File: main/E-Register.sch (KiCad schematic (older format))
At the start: 19 parts, among them U71 74LS245, U72 74LS173, U73 74LS173

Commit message: Replot main with symbols
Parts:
- renumbered D46 to D38, D47 to D39, D48 to D40, D49 to D41, D50 to D42, D51 to D43, D52 to D44, D53 to D45, R52 to R44, R53 to R45, R54 to R46, R55 to R47, R56 to R48, R57 to R49, R58 to R50, R59 to R51, U71 to U56, U72 to U57, U73 to U58
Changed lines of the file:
@@
 Sheet 15 26
 Title "E Register"
-Date "2019-11-13"
+Date "2019-11-17"
 Rev "v1.0"
 Comp "Christopher Milan"
@@
 AR Path="/5D9C73BD/5DA2C3AD" Ref="U?"  Part="1"
 AR Path="/5D9E8388/5DA2C3AD" Ref="U?"  Part="1"
-AR Path="/5DA98D6D/5DA9A55B/5DA2C3AD" Ref="U71"  Part="1"
-F 0 "U71" V 2946 2156 50  0000 R CNN
+AR Path="/5DA98D6D/5DA9A55B/5DA2C3AD" Ref="U56"  Part="1"
+F 0 "U56" V 2946 2156 50  0000 R CNN
 F 1 "74LS245" V 2855 2156 50  0000 R CNN
 F 2 "" H 2900 3000 50  0001 C CNN
@@
 AR Path="/5D9C73BD/5DA2C3DA" Ref="U?"  Part="1"
 AR Path="/5D9E8388/5DA2C3DA" Ref="U?"  Part="1"
-AR Path="/5DA98D6D/5DA9A55B/5DA2C3DA" Ref="U73"  Part="1"
-F 0 "U73" V 7454 3944 50  0000 L CNN
+AR Path="/5DA98D6D/5DA9A55B/5DA2C3DA" Ref="U58"  Part="1"
+F 0 "U58" V 7454 3944 50  0000 L CNN
 F 1 "74LS173" V 7545 3944 50  0000 L CNN
 F 2 "" H 7500 3000 50  0001 C CNN
@@
 AR Path="/5D9C73BD/5DA2C404" Ref="D?"  Part="1"
 AR Path="/5D9E8388/5DA2C404" Ref="D?"  Part="1"
-AR Path="/5DA98D6D/5DA9A55B/5DA2C404" Ref="D46"  Part="1"
-F 0 "D46" V 3489 5383 50  0000 R CNN
+AR Path="/5DA98D6D/5DA9A55B/5DA2C404" Ref="D38"  Part="1"
+F 0 "D38" V 3489 5383 50  0000 R CNN
 F 1 "LED" V 3398 5383 50  0000 R CNN
 F 2 "" H 3450 5500 50  0001 C CNN
@@
 AR Path="/5D9C73BD/5DA2C40A" Ref="D?"  Part="1"
 AR Path="/5D9E8388/5DA2C40A" Ref="D?"  Part="1"
-AR Path="/5DA98D6D/5DA9A55B/5DA2C40A" Ref="D47"  Part="1"
-F 0 "D47" V 3839 5383 50  0000 R CNN
+AR Path="/5DA98D6D/5DA9A55B/5DA2C40A" Ref="D39"  Part="1"
+F 0 "D39" V 3839 5383 50  0000 R CNN
 F 1 "LED" V 3748 5383 50  0000 R CNN
 F 2 "" H 3800 5500 50  0001 C CNN
@@
 AR Path="/5D9C73BD/5DA2C410" Ref="D?"  Part="1"
 AR Path="/5D9E8388/5DA2C410" Ref="D?"  Part="1"
-AR Path="/5DA98D6D/5DA9A55B/5DA2C410" Ref="D48"  Part="1"
-F 0 "D48" V 4189 5383 50  0000 R CNN
+AR Path="/5DA98D6D/5DA9A55B/5DA2C410" Ref="D40"  Part="1"
+F 0 "D40" V 4189 5383 50  0000 R CNN
 F 1 "LED" V 4098 5383 50  0000 R CNN
 F 2 "" H 4150 5500 50  0001 C CNN
@@
 AR Path="/5D9C73BD/5DA2C416" Ref="D?"  Part="1"
 AR Path="/5D9E8388/5DA2C416" Ref="D?"  Part="1"
-AR Path="/5DA98D6D/5DA9A55B/5DA2C416" Ref="D49"  Part="1"
-F 0 "D49" V 4539 5383 50  0000 R CNN
+AR Path="/5DA98D6D/5DA9A55B/5DA2C416" Ref="D41"  Part="1"
+F 0 "D41" V 4539 5383 50  0000 R CNN
 F 1 "LED" V 4448 5383 50  0000 R CNN
 F 2 "" H 4500 5500 50  0001 C CNN
@@
 AR Path="/5D9C73BD/5DA2C41C" Ref="D?"  Part="1"
 AR Path="/5D9E8388/5DA2C41C" Ref="D?"  Part="1"
-AR Path="/5DA98D6D/5DA9A55B/5DA2C41C" Ref="D50"  Part="1"
-F 0 "D50" V 4889 5383 50  0000 R CNN
+AR Path="/5DA98D6D/5DA9A55B/5DA2C41C" Ref="D42"  Part="1"
+F 0 "D42" V 4889 5383 50  0000 R CNN
 F 1 "LED" V 4798 5383 50  0000 R CNN
 F 2 "" H 4850 5500 50  0001 C CNN
@@
 AR Path="/5D9C73BD/5DA2C422" Ref="D?"  Part="1"
 AR Path="/5D9E8388/5DA2C422" Ref="D?"  Part="1"
-AR Path="/5DA98D6D/5DA9A55B/5DA2C422" Ref="D51"  Part="1"
-F 0 "D51" V 5239 5383 50  0000 R CNN
+AR Path="/5DA98D6D/5DA9A55B/5DA2C422" Ref="D43"  Part="1"
+F 0 "D43" V 5239 5383 50  0000 R CNN
 F 1 "LED" V 5148 5383 50  0000 R CNN
 F 2 "" H 5200 5500 50  0001 C CNN
@@
 AR Path="/5D9C73BD/5DA2C428" Ref="D?"  Part="1"
 AR Path="/5D9E8388/5DA2C428" Ref="D?"  Part="1"
-AR Path="/5DA98D6D/5DA9A55B/5DA2C428" Ref="D52"  Part="1"
-F 0 "D52" V 5589 5383 50  0000 R CNN
+AR Path="/5DA98D6D/5DA9A55B/5DA2C428" Ref="D44"  Part="1"
+F 0 "D44" V 5589 5383 50  0000 R CNN
 F 1 "LED" V 5498 5383 50  0000 R CNN
 F 2 "" H 5550 5500 50  0001 C CNN
@@
 AR Path="/5D9C73BD/5DA2C42E" Ref="D?"  Part="1"
 AR Path="/5D9E8388/5DA2C42E" Ref="D?"  Part="1"
-AR Path="/5DA98D6D/5DA9A55B/5DA2C42E" Ref="D53"  Part="1"
-F 0 "D53" V 5939 5383 50  0000 R CNN
+AR Path="/5DA98D6D/5DA9A55B/5DA2C42E" Ref="D45"  Part="1"
+F 0 "D45" V 5939 5383 50  0000 R CNN
 F 1 "LED" V 5848 5383 50  0000 R CNN
 F 2 "" H 5900 5500 50  0001 C CNN
@@
 AR Path="/5D9C73BD/5DA2C44A" Ref="R?"  Part="1"
 AR Path="/5D9E8388/5DA2C44A" Ref="R?"  Part="1"
-AR Path="/5DA98D6D/5DA9A55B/5DA2C44A" Ref="R52"  Part="1"
-F 0 "R52" H 3520 6096 50  0000 L CNN
+AR Path="/5DA98D6D/5DA9A55B/5DA2C44A" Ref="R44"  Part="1"
+F 0 "R44" H 3520 6096 50  0000 L CNN
 F 1 "220" H 3520 6005 50  0000 L CNN
 F 2 "" V 3380 6050 50  0001 C CNN
@@
 AR Path="/5D9C73BD/5DA2C450" Ref="R?"  Part="1"
 AR Path="/5D9E8388/5DA2C450" Ref="R?"  Part="1"
-AR Path="/5DA98D6D/5DA9A55B/5DA2C450" Ref="R53"  Part="1"
-F 0 "R53" H 3870 6096 50  0000 L CNN
+AR Path="/5DA98D6D/5DA9A55B/5DA2C450" Ref="R45"  Part="1"
+F 0 "R45" H 3870 6096 50  0000 L CNN
 F 1 "220" H 3870 6005 50  0000 L CNN
 F 2 "" V 3730 6050 50  0001 C CNN
@@
 AR Path="/5D9C73BD/5DA2C456" Ref="R?"  Part="1"
 AR Path="/5D9E8388/5DA2C456" Ref="R?"  Part="1"
-AR Path="/5DA98D6D/5DA9A55B/5DA2C456" Ref="R54"  Part="1"
-F 0 "R54" H 4220 6096 50  0000 L CNN
+AR Path="/5DA98D6D/5DA9A55B/5DA2C456" Ref="R46"  Part="1"
+F 0 "R46" H 4220 6096 50  0000 L CNN
 F 1 "220" H 4220 6005 50  0000 L CNN
 F 2 "" V 4080 6050 50  0001 C CNN
@@
 AR Path="/5D9C73BD/5DA2C45C" Ref="R?"  Part="1"
 AR Path="/5D9E8388/5DA2C45C" Ref="R?"  Part="1"
-AR Path="/5DA98D6D/5DA9A55B/5DA2C45C" Ref="R55"  Part="1"
-F 0 "R55" H 4570 6096 50  0000 L CNN
+AR Path="/5DA98D6D/5DA9A55B/5DA2C45C" Ref="R47"  Part="1"
+F 0 "R47" H 4570 6096 50  0000 L CNN
 F 1 "220" H 4570 6005 50  0000 L CNN
 F 2 "" V 4430 6050 50  0001 C CNN
@@
 AR Path="/5D9C73BD/5DA2C462" Ref="R?"  Part="1"
 AR Path="/5D9E8388/5DA2C462" Ref="R?"  Part="1"
-AR Path="/5DA98D6D/5DA9A55B/5DA2C462" Ref="R56"  Part="1"
-F 0 "R56" H 4920 6096 50  0000 L CNN
+AR Path="/5DA98D6D/5DA9A55B/5DA2C462" Ref="R48"  Part="1"
+F 0 "R48" H 4920 6096 50  0000 L CNN
 F 1 "220" H 4920 6005 50  0000 L CNN
 F 2 "" V 4780 6050 50  0001 C CNN
@@
 AR Path="/5D9C73BD/5DA2C468" Ref="R?"  Part="1"
 AR Path="/5D9E8388/5DA2C468" Ref="R?"  Part="1"
-AR Path="/5DA98D6D/5DA9A55B/5DA2C468" Ref="R57"  Part="1"
-F 0 "R57" H 5270 6096 50  0000 L CNN
+AR Path="/5DA98D6D/5DA9A55B/5DA2C468" Ref="R49"  Part="1"
+F 0 "R49" H 5270 6096 50  0000 L CNN
 F 1 "220" H 5270 6005 50  0000 L CNN
 F 2 "" V 5130 6050 50  0001 C CNN
@@
 AR Path="/5D9C73BD/5DA2C46E" Ref="R?"  Part="1"
 AR Path="/5D9E8388/5DA2C46E" Ref="R?"  Part="1"
-AR Path="/5DA98D6D/5DA9A55B/5DA2C46E" Ref="R58"  Part="1"
-F 0 "R58" H 5620 6096 50  0000 L CNN
+AR Path="/5DA98D6D/5DA9A55B/5DA2C46E" Ref="R50"  Part="1"
+F 0 "R50" H 5620 6096 50  0000 L CNN
 F 1 "220" H 5620 6005 50  0000 L CNN
 F 2 "" V 5480 6050 50  0001 C CNN
@@
 AR Path="/5D9C73BD/5DA2C474" Ref="R?"  Part="1"
 AR Path="/5D9E8388/5DA2C474" Ref="R?"  Part="1"
-AR Path="/5DA98D6D/5DA9A55B/5DA2C474" Ref="R59"  Part="1"
-F 0 "R59" H 5970 6096 50  0000 L CNN
+AR Path="/5DA98D6D/5DA9A55B/5DA2C474" Ref="R51"  Part="1"
+F 0 "R51" H 5970 6096 50  0000 L CNN
 F 1 "220" H 5970 6005 50  0000 L CNN
 F 2 "" V 5830 6050 50  0001 C CNN
@@
 AR Path="/5D9C73BD/5DA2C4C5" Ref="U?"  Part="1"
 AR Path="/5D9E8388/5DA2C4C5" Ref="U?"  Part="1"
-AR Path="/5DA98D6D/5DA9A55B/5DA2C4C5" Ref="U72"  Part="1"
-F 0 "U72" V 5204 3944 50  0000 L CNN
+AR Path="/5DA98D6D/5DA9A55B/5DA2C4C5" Ref="U57"  Part="1"
+F 0 "U57" V 5204 3944 50  0000 L CNN
 F 1 "74LS173" V 5295 3944 50  0000 L CNN
 F 2 "" H 5250 3000 50  0001 C CNN

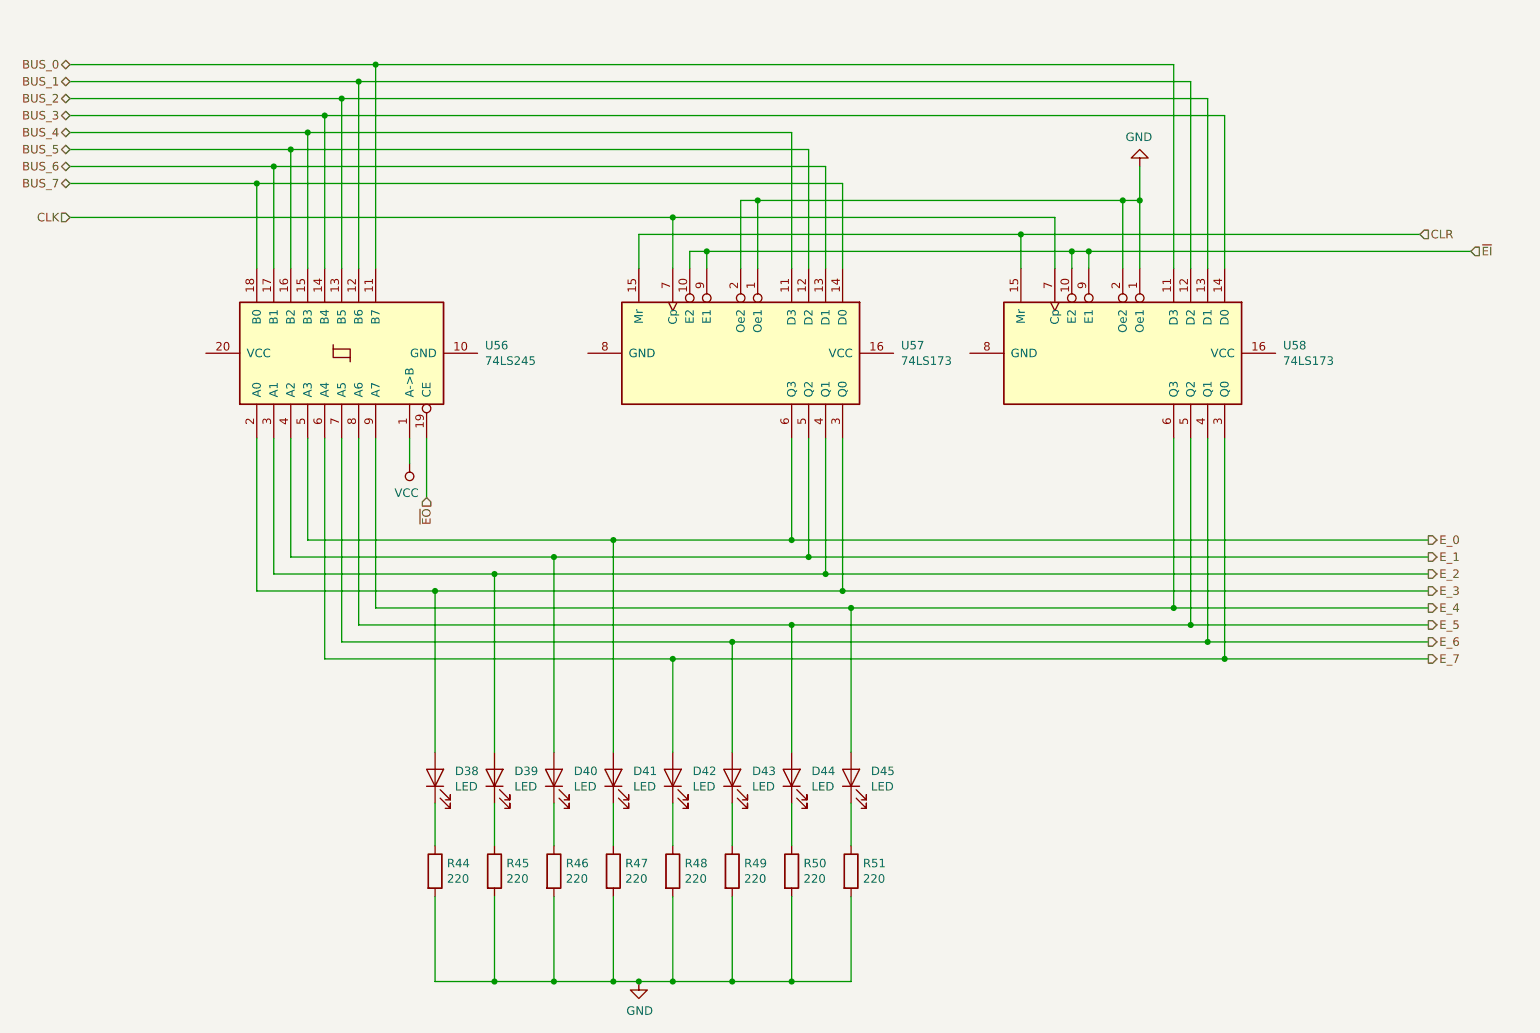
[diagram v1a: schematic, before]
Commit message: Switch to using 74LS377 in place of two 74LS173
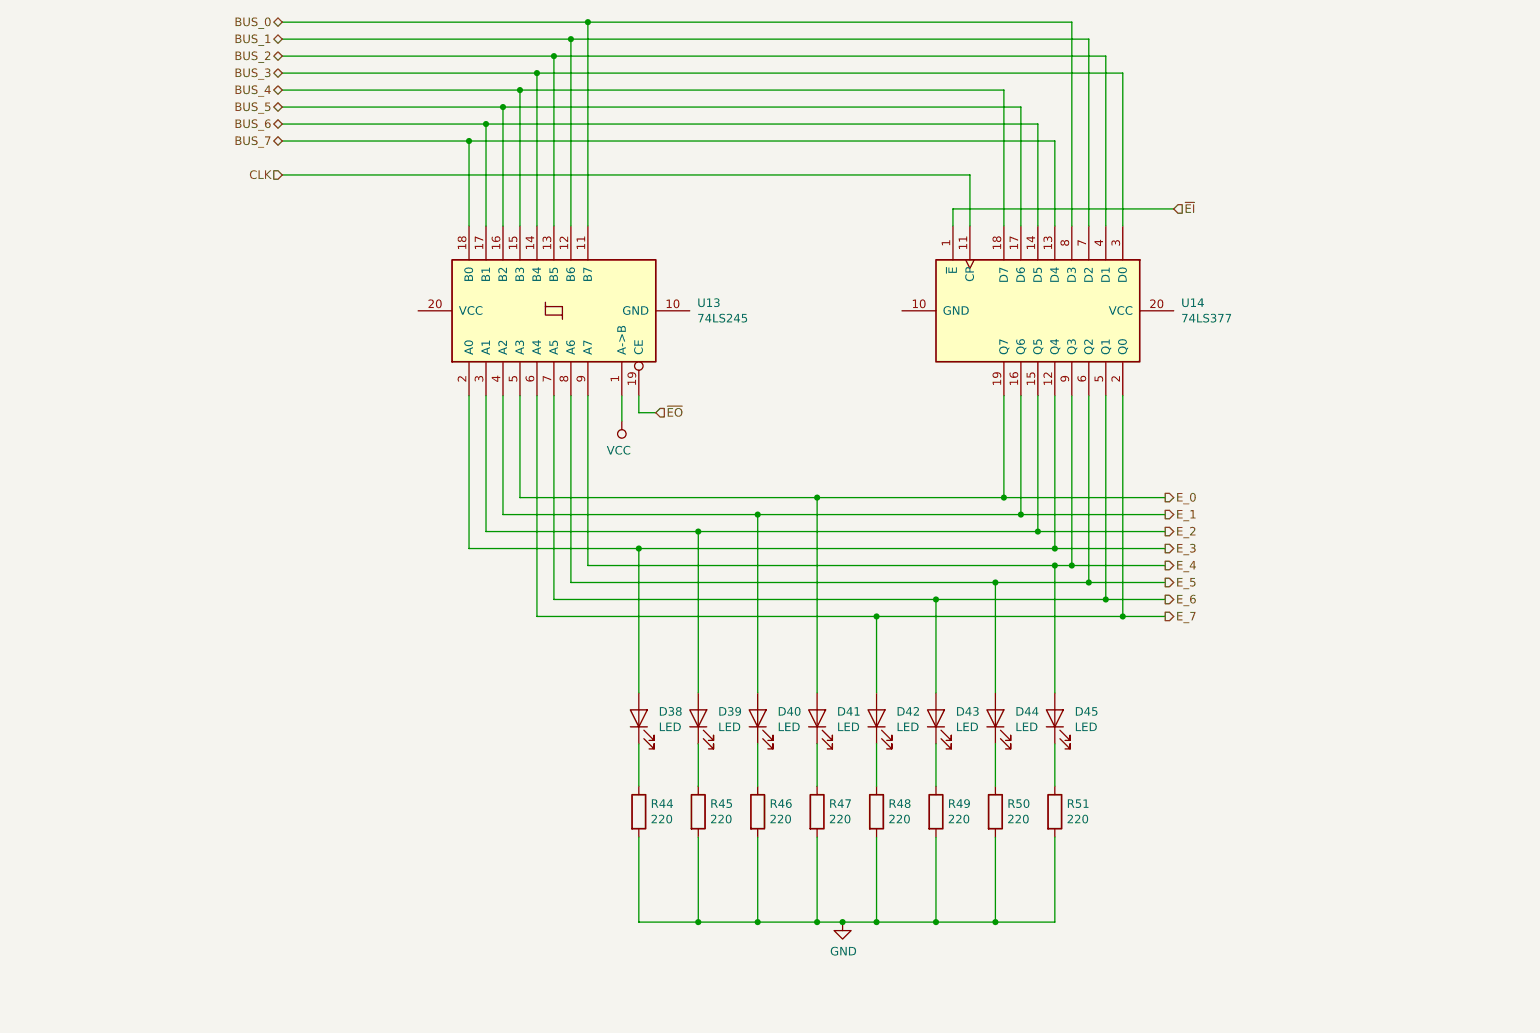
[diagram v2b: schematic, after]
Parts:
- removed U56: 74LS245, symbol 74xx:74LS245
- removed U57, U58: 74LS173, symbol 74xx:74LS173
- added U13: 74LS245, symbol 74xx:74LS245
- added U14: 74LS377, symbol 74xx:74LS377
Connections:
- net BUS_0: now also U13.11 (B7), U14.8 (D3)
- net BUS_1: now also U13.12 (B6), U14.7 (D2)
- net BUS_2: now also U13.13 (B5), U14.4 (D1)
- net BUS_3: now also U13.14 (B4), U14.3 (D0)
- net BUS_4: now also U13.15 (B3), U14.18 (D7)
- net BUS_5: now also U13.16 (B2), U14.17 (D6)
- net BUS_6: now also U13.17 (B1), U14.14 (D5)
- net BUS_7: now also U13.18 (B0), U14.13 (D4)
- net CLK: now also U14.11 (CP)
- net E_0: now also U13.5 (A3), U14.19 (Q7)
- net E_1: now also U13.4 (A2), U14.16 (Q6)
- net E_2: now also U13.3 (A1), U14.15 (Q5)
- net E_3: now also U13.2 (A0), U14.12 (Q4)
- net E_4: now also U13.9 (A7), U14.9 (Q3)
- net E_5: now also U13.8 (A6), U14.6 (Q2)
- net E_6: now also U13.7 (A5), U14.5 (Q1)
- net E_7: now also U13.6 (A4), U14.2 (Q0)
- net VCC: now also U13.1 (A->B)
- net ~EI~: now also U14.1 (~E)
- net ~EO~: now also U13.19 (CE)
